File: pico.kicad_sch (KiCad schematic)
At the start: 4 parts, among them U3 Pico

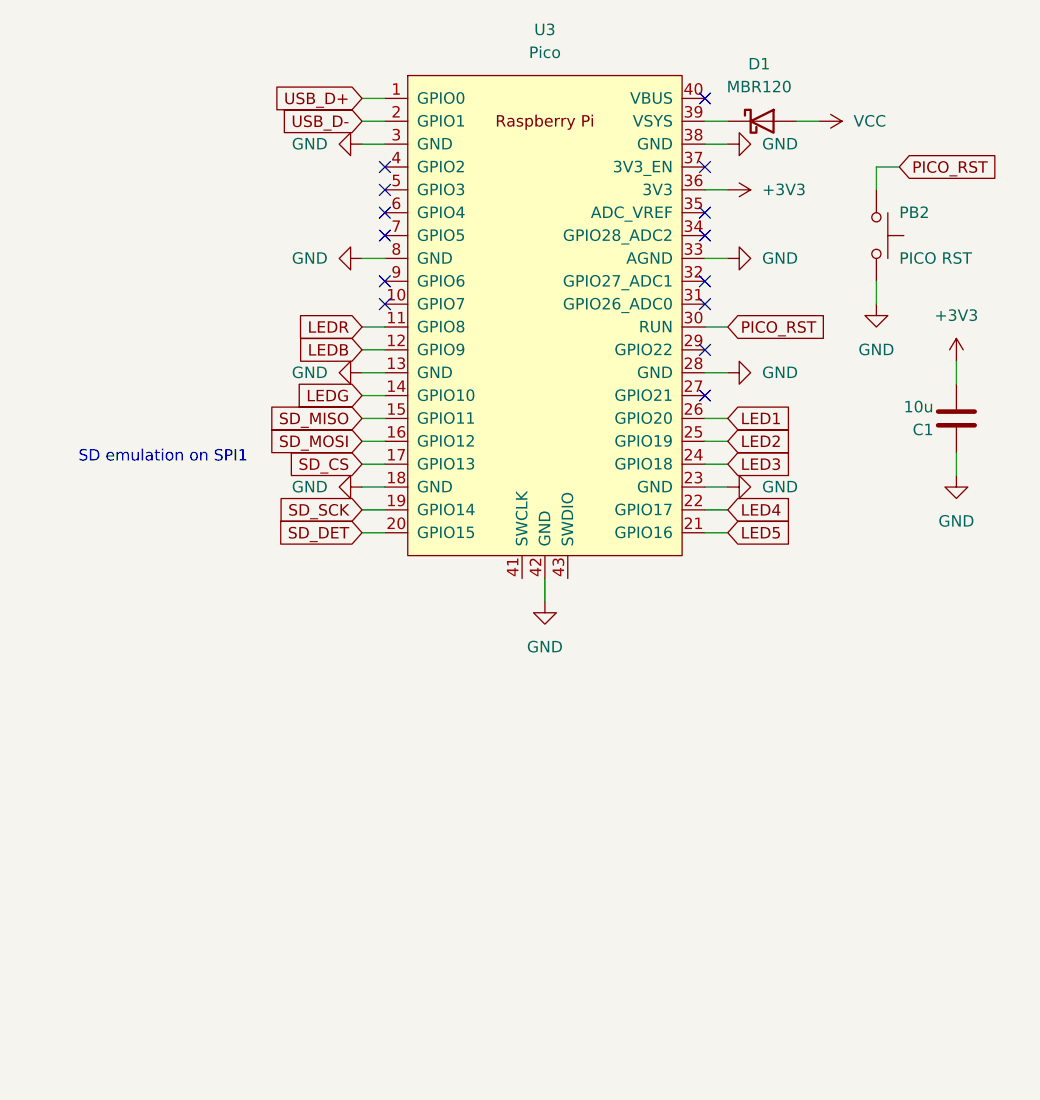
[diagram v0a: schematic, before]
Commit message: feature: add pico debug connections, testpoints
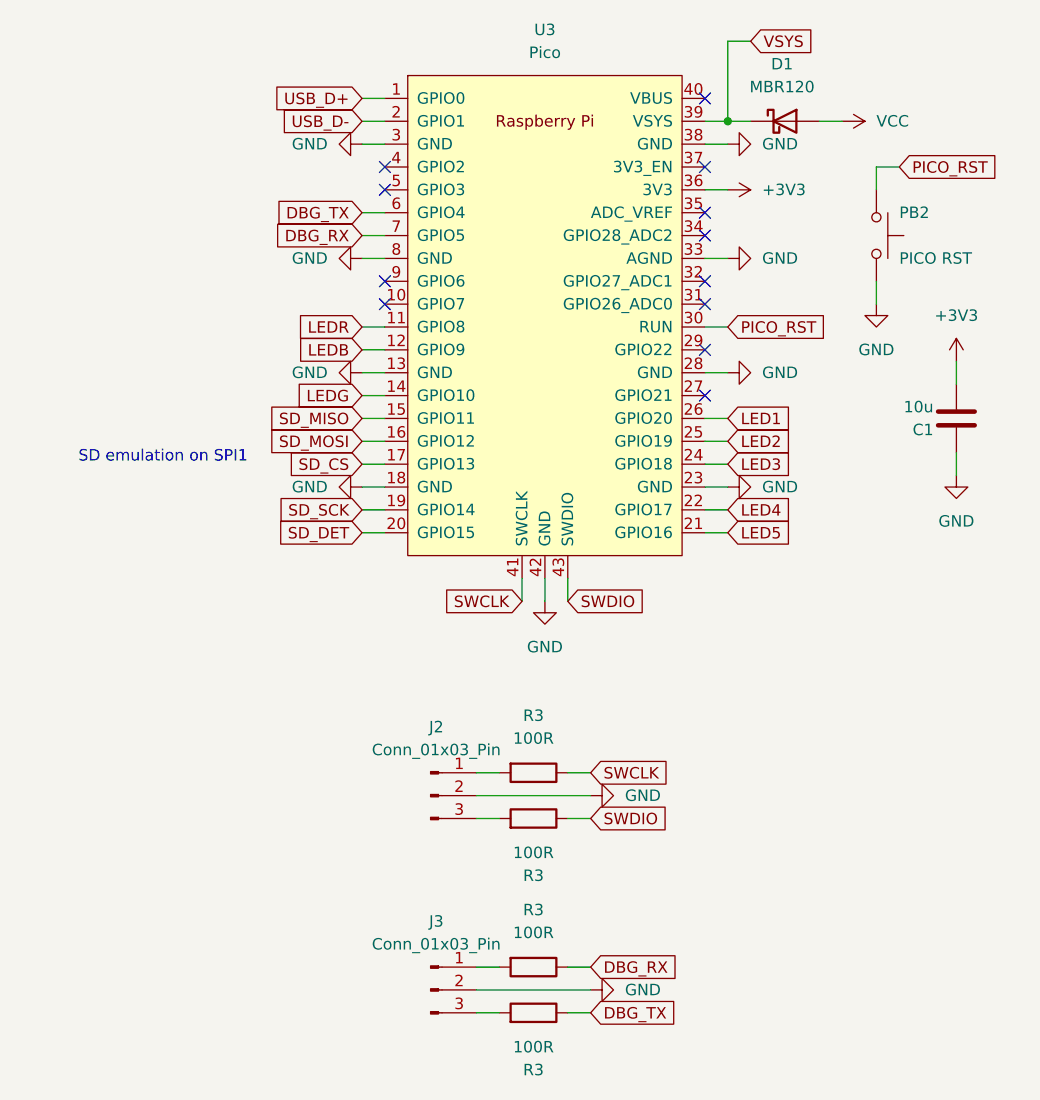
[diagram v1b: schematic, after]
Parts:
- added J2, J3: Conn_01x03_Pin, Gigahawk:JST_SH_BM03B-SRSS-TB_1x03-1MP_P1.00mm_Vertical, symbol Connector:Conn_01x03_Pin
- added R3 (x4): 100R, Resistor_SMD:R_0805_2012Metric_Pad1.20x1.40mm_HandSolder, symbol Device:R
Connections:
- net GND: now also J2.2 (Pin_2), J3.2 (Pin_2)
- net VSYS: now reaches D1.1 (K), U3.39 (VSYS)
- net SWCLK: now reaches U3.41 (SWCLK)
- net SWCLK: now also R3.1
- net SWDIO: now reaches U3.43 (SWDIO)
- net SWDIO: now also R3.1
- net DBG_TX: now reaches U3.6 (GPIO4)
- net DBG_TX: now also R3.1
- net DBG_RX: now reaches U3.7 (GPIO5)
- net DBG_RX: now also R3.1
- new net: J3.3 (Pin_3), R3.2
- new net: J2.3 (Pin_3), R3.2
- new net: J2.1 (Pin_1), R3.2
- new net: J3.1 (Pin_1), R3.2
- no-connect marks 14 -> 12
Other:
- moved on the sheet: D1

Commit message: bom: update bom
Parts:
- J2, J3: Digikey (none) -> 455-BM03B-SRSS-TBCT-ND
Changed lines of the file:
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@@
+      (effects (font (size 1.27 1.27)) hide)
+    )
+    (property "Digikey" "455-BM03B-SRSS-TBCT-ND" (at 62.23 121.92 0)
       (effects (font (size 1.27 1.27)) hide)
     )
@@
       (effects (font (size 1.27 1.27)) hide)
     )
+    (property "Digikey" "455-BM03B-SRSS-TBCT-ND" (at 62.23 143.51 0)
+      (effects (font (size 1.27 1.27)) hide)
+    )

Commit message: schem: export revision info to all sheets
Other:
- title: (none) -> RepRapDiscount.com Smart Controller
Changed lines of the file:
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@@
 (kicad_sch (version 20230121) (generator eeschema)
-  (paper "A4")
+  (paper "A")
+  (title_block
+    (title "RepRapDiscount.com Smart Controller")
+    (date "${DATE}")
+    (rev "${TAG} (${HASH})")
+  )
   (junction (at 95.25 46.99) (diameter 0) (color 0 0 0 0)
   )
